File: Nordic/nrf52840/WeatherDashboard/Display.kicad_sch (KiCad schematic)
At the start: 14 parts, among them Q1 BSS138

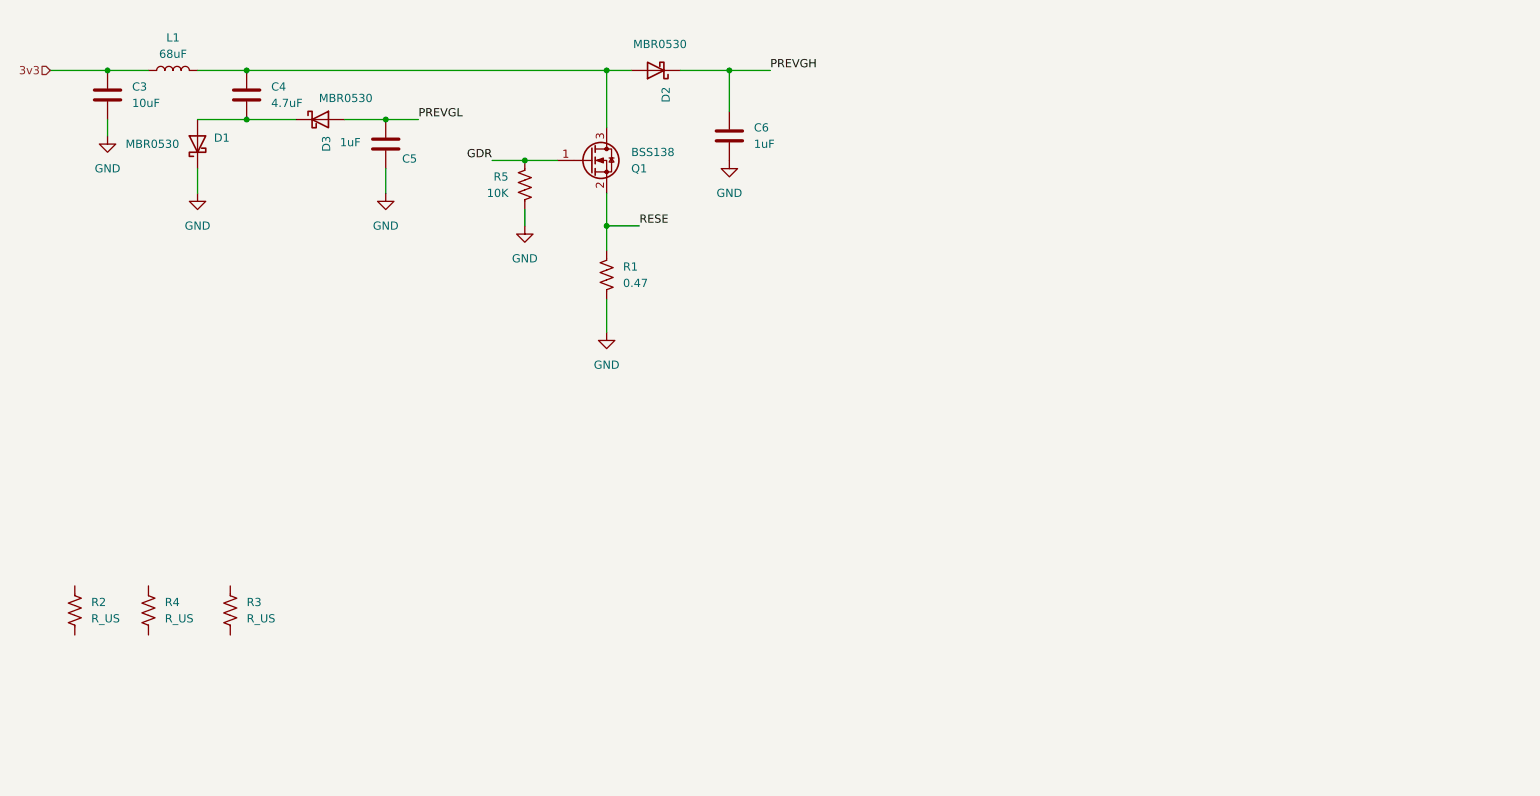
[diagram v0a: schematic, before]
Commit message: Display
Added fpc connector and power enable components
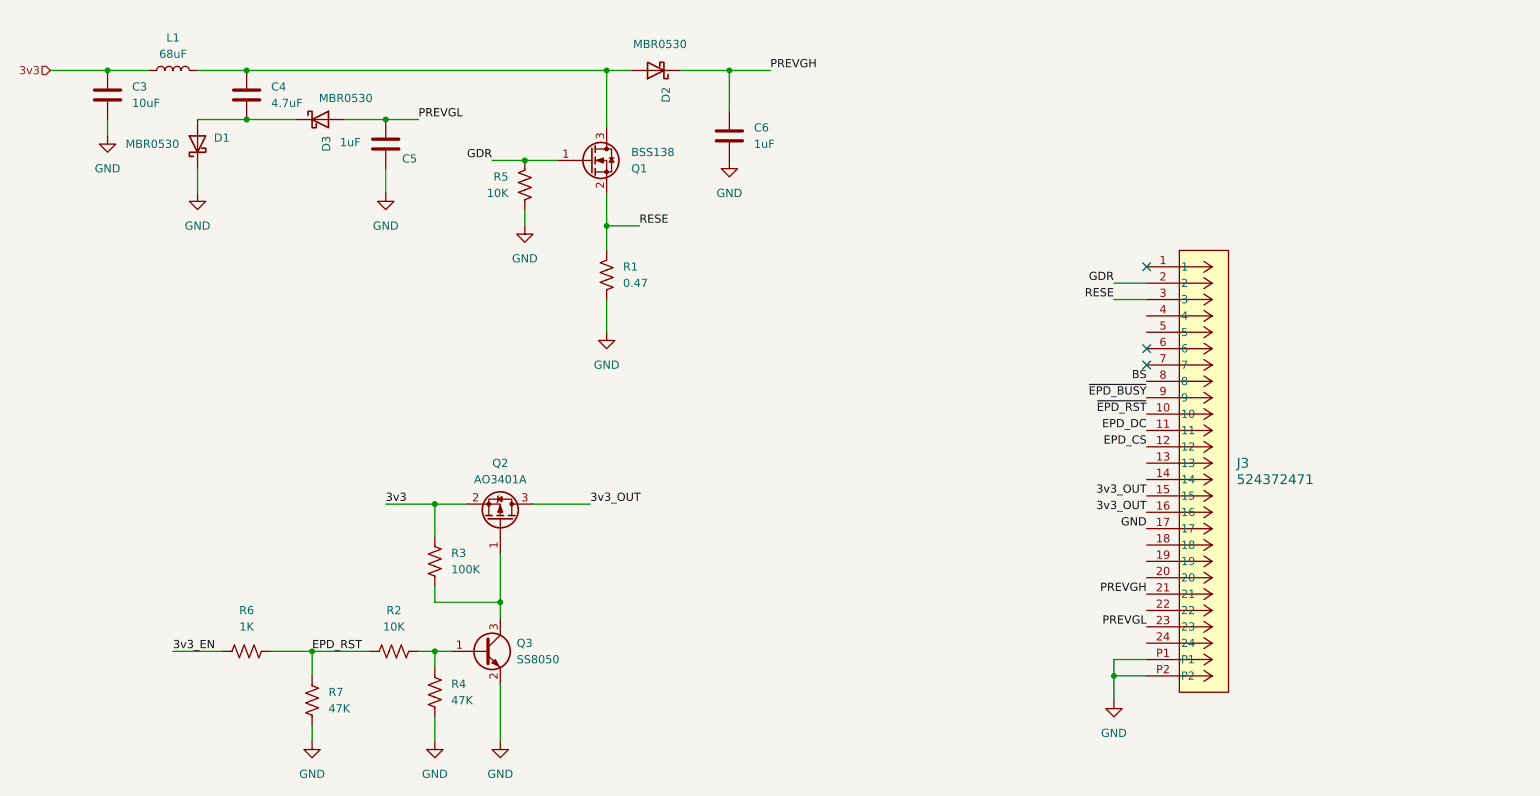
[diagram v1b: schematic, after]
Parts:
- added J3: 524372471, User_Footprint:CON_524372471_MOL, symbol _Connectors:524372471
- added Q2: AO3401A, Package_TO_SOT_SMD:SOT-23, symbol Transistor_FET:AO3401A
- added Q3: SS8050, Package_TO_SOT_SMD:SOT-23_Handsoldering, symbol Transistor_BJT:SS8050
- added R6: 1K, Resistor_SMD:R_0402_1005Metric_Pad0.72x0.64mm_HandSolder, symbol Device:R_US
- added R7: 47K, Resistor_SMD:R_0402_1005Metric_Pad0.72x0.64mm_HandSolder, symbol Device:R_US
- R2: value R_US -> 10K
- R3: value R_US -> 100K
- R4: value R_US -> 47K
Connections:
- net 3v3: now also R3.1, Q2.2 (S)
- net GDR: now also J3.2
- net GND: now also R4.2, J3.17, J3.P1, J3.P2, Q3.2 (E), R7.1
- net PREVGH: now also J3.21
- net PREVGL: now also J3.23
- net RESE: now also J3.3
- net at R3.2: now also Q2.1 (G), Q3.3 (C)
- net EPD_RST: now reaches R2.1
- net EPD_RST: now also R6.1, R7.2
- net at R2.2: now also R4.1, Q3.1 (B)
- new net 3v3_EN: R6.2
- new net 3v3_OUT: J3.15, J3.16, Q2.3 (D)
- new net BS: J3.8
- new net EPD_CS: J3.12
- new net EPD_DC: J3.11
- new net ~{EPD_BUSY}: J3.9
- new net ~{EPD_RST}: J3.10
- no-connect marks 0 -> 3
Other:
- moved on the sheet: R2, R3, R4

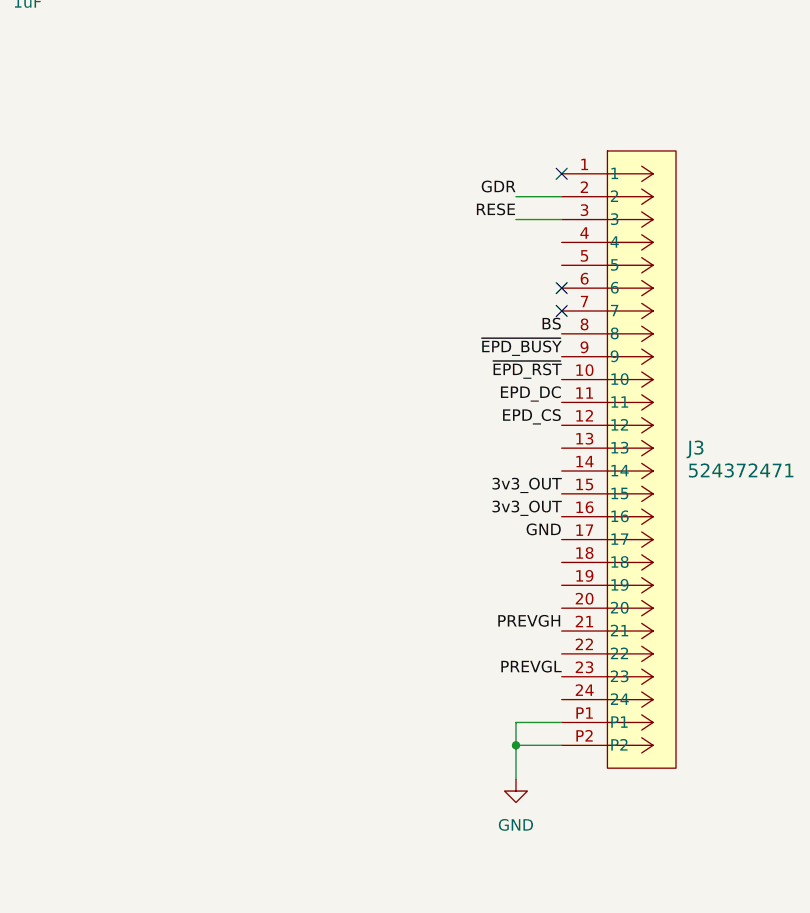
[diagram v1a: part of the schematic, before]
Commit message: pcie
added pcie connector
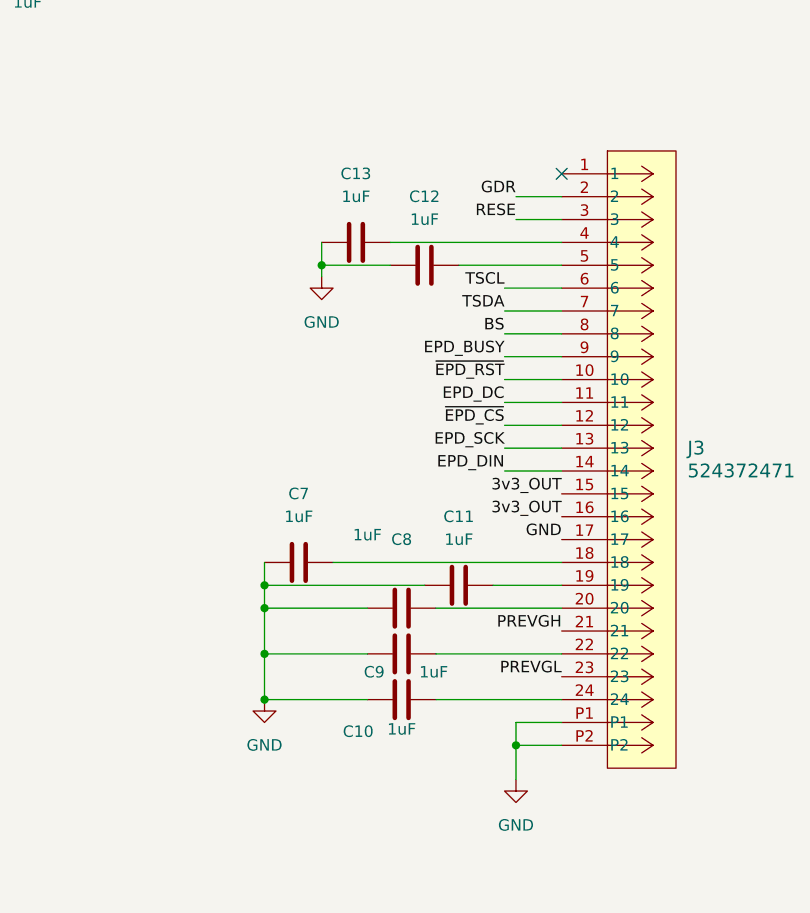
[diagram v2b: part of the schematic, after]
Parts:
- added C10, C11, C12, C13, C7, C8, C9: 1uF, Capacitor_SMD:C_0402_1005Metric_Pad0.74x0.62mm_HandSolder, symbol Device:C
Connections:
- net GND: now also C10.1, C11.1, C12.1, C13.1, C7.1, C8.1, C9.1
- net EPD_SCK: now reaches J3.13
- net EPD_DIN: now reaches J3.14
- net at J3.18: now also C7.2
- net at J3.19: now also C11.2
- net at J3.20: now also C8.2
- net at J3.22: now also C9.2
- net at J3.24: now also C10.2
- net at J3.4: now also C13.2
- net at J3.5: now also C12.2
- net TSCL: now reaches J3.6
- net TSDA: now reaches J3.7
- net EPD_CS renamed ~{EPD_CS}
- net ~{EPD_BUSY} renamed EPD_BUSY
- no-connect marks 3 -> 1

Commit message: pcie connector
Add connectins to the pcie connector
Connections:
- net EPD_BUSY: now also J3.14; no longer J3.9
- net EPD_DC: now also J3.12; no longer J3.11
- net EPD_DIN: now also J3.9; no longer J3.14
- net EPD_SCK: now also J3.10; no longer J3.13
- net TSCL: now also J3.7; no longer J3.6
- net TSDA: now also J3.6; no longer J3.7
- net ~{EPD_CS}: now also J3.11; no longer J3.12
- net ~{EPD_RST}: now also J3.13; no longer J3.10
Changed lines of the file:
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@@
-		)
-	)
-	(label "EPD_BUSY"
-		(at 187.96 85.09 180)
-		(effects
-			(font
-				(size 1.27 1.27)
-			)
-			(justify right bottom)
-		)
-	)
-	(label "3v3_EN"
-		(at 43.18 124.46 0)
-		(effects
-			(font
-				(size 1.27 1.27)
-			)
-			(justify left bottom)
-		)
-	)
-	(label "BS"
-		(at 187.96 82.55 180)
-		(effects
-			(font
-				(size 1.27 1.27)
-			)
-			(justify right bottom)
 		)
 	)
@@
 		)
 	)
-	(label "~{EPD_CS}"
-		(at 187.96 92.71 180)
-		(effects
-			(font
-				(size 1.27 1.27)
-			)
-			(justify right bottom)
-		)
-	)
 	(label "PREVGH"
 		(at 194.31 115.57 180)
@@
 		)
 	)
-	(label "EPD_DIN"
-		(at 187.96 97.79 180)
-		(effects
-			(font
-				(size 1.27 1.27)
-			)
-			(justify right bottom)
-		)
-	)
 	(label "GDR"
 		(at 92.71 48.26 180)
@@
 		)
 	)
-	(label "TSDA"
-		(at 187.96 80.01 180)
-		(effects
-			(font
-				(size 1.27 1.27)
-			)
-			(justify right bottom)
-		)
-	)
 	(label "GDR"
 		(at 189.23 67.31 180)
@@
 		)
 	)
-	(label "EPD_SCK"
-		(at 187.96 95.25 180)
-		(effects
-			(font
-				(size 1.27 1.27)
-			)
-			(justify right bottom)
-		)
-	)
 	(label "PREVGL"
 		(at 194.31 120.65 180)
@@
 		)
 	)
-	(label "TSCL"
-		(at 187.96 77.47 180)
-		(effects
-			(font
-				(size 1.27 1.27)
-			)
-			(justify right bottom)
-		)
-	)
 	(label "3v3"
 		(at 76.2 101.6 0)
@@
 		)
 	)
-	(label "~{EPD_RST}"
-		(at 187.96 87.63 180)
-		(effects
-			(font
-				(size 1.27 1.27)
-			)
-			(justify right bottom)
-		)
-	)
 	(label "RESE"
 		(at 189.23 69.85 180)
@@
 		)
 	)
-	(label "EPD_DC"
+	(hierarchical_label "BS"
+		(shape input)
+		(at 187.96 82.55 180)
+		(effects
+			(font
+				(size 1.27 1.27)
+			)
+			(justify right)
+		)
+	)
+	(hierarchical_label "EPD_DIN"
+		(shape input)
+		(at 187.96 85.09 180)
+		(effects
+			(font
+				(size 1.27 1.27)
+			)
+			(justify right)
+		)
+	)
+	(hierarchical_label "3v3"
+		(shape input)
+		(at 24.13 34.29 180)
+		(effects
+			(font
+				(size 1.27 1.27)
+			)
+			(justify right)
+		)
+	)
+	(hierarchical_label "GND"
+		(shape input)
+		(at 161.29 118.11 180)
+		(effects
+			(font
+				(size 1.27 1.27)
+			)
+			(justify right)
+		)
+	)
+	(hierarchical_label "~{EPD_RST}"
+		(shape input)
+		(at 187.96 95.25 180)
+		(effects
+			(font
+				(size 1.27 1.27)
+			)
+			(justify right)
+		)
+	)
+	(hierarchical_label "~{EPD_CS}"
+		(shape input)
 		(at 187.96 90.17 180)
 		(effects
@@
 				(size 1.27 1.27)
 			)
-			(justify right bottom)
-		)
-	)
-	(hierarchical_label "3v3"
-		(shape input)
-		(at 24.13 34.29 180)
-		(effects
-			(font
+			(justify right)
+		)
+	)
+	(hierarchical_label "EPD_DC"
+		(shape input)
+		(at 187.96 92.71 180)
+		(effects
+			(font
+				(size 1.27 1.27)
+			)
+			(justify right)
+		)
+	)
+	(hierarchical_label "EPD_BUSY"
+		(shape input)
+		(at 187.96 97.79 180)
+		(effects
+			(font
+				(size 1.27 1.27)
+			)
+			(justify right)
+		)
+	)
+	(hierarchical_label "TSDA"
+		(shape input)
+		(at 187.96 77.47 180)
+		(effects
+			(font
+				(size 1.27 1.27)
+			)
+			(justify right)
+		)
+	)
+	(hierarchical_label "TSCL"
+		(shape input)
+		(at 187.96 80.01 180)
+		(effects
+			(font
+				(size 1.27 1.27)
+			)
+			(justify right)
+		)
+	)
+	(hierarchical_label "3v3_EN"
+		(shape input)
+		(at 43.18 124.46 180)
+		(effects
+			(font
+				(size 1.27 1.27)
+			)
+			(justify right)
+		)
+	)
+	(hierarchical_label "EPD_SCK"
+		(shape input)
+		(at 187.96 87.63 180)
+		(effects
+			(font

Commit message: Layout
layout update
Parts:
- removed L1: 68uF, symbol Device:L
- added L1: SDE0805A-680K, User_Footprint:IND_SDE0805A-680K, symbol _Misc_Symbols:SDE0805A-680K
- added R10, R9: 0, Resistor_SMD:R_0402_1005Metric_Pad0.72x0.64mm_HandSolder, symbol Device:R_US
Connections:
- net 3v3: now also L1.1, R9.1
- net GND: now also R10.2
- net at C4.1, D2.2 (A), Q1.3 (D): now also L1.2
- net BS: no longer names the net of J3.8
- net BS: now also R10.1, R9.2
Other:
- moved on the sheet: C3

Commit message: layout
update layout for the pcie connector
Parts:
- added R17, R18: 10K, Resistor_SMD:R_0402_1005Metric_Pad0.72x0.64mm_HandSolder, symbol Device:R_US
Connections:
- net 3v3: now also R17.2, R18.2
- net TSCL: now also R18.1
- net TSDA: now also R17.1
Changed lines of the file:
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@@
+	)
+	(junction
+		(at 241.3 44.45)
+		(diameter 0)
+		(color 0 0 0 0)
 	)
 	(junction
@@
 	(wire
 		(pts
+			(xy 234.95 52.07) (xy 234.95 55.88)
+		)
+		(stroke
+			(width 0)
+			(type default)
+		)
+	)
+	(wire
+		(pts
 			(xy 64.77 135.89) (xy 64.77 138.43)
 		)
@@
 	(wire
 		(pts
+			(xy 246.38 52.07) (xy 246.38 55.88)
+		)
+		(stroke
+			(width 0)
+			(type default)
+		)
+	)
+	(wire
+		(pts
 			(xy 81.28 124.46) (xy 83.82 124.46)
 		)
@@
 	(wire
 		(pts
+			(xy 234.95 55.88) (xy 233.68 55.88)
+		)
+		(stroke
+			(width 0)
+			(type default)
+		)
+	)
+	(wire
+		(pts
 			(xy 189.23 67.31) (xy 194.31 67.31)
 		)
@@
 	(wire
 		(pts
+			(xy 234.95 44.45) (xy 241.3 44.45)
+		)
+		(stroke
+			(width 0)
+			(type default)
+		)
+	)
+	(wire
+		(pts
 			(xy 187.96 87.63) (xy 194.31 87.63)
 		)
@@
 	(wire
 		(pts
+			(xy 246.38 55.88) (xy 247.65 55.88)
+		)
+		(stroke
+			(width 0)
+			(type default)
+		)
+	)
+	(wire
+		(pts
 			(xy 180.34 118.11) (xy 194.31 118.11)
 		)
@@
 	(wire
 		(pts
+			(xy 241.3 38.1) (xy 241.3 44.45)
+		)
+		(stroke
+			(width 0)
+			(type default)
+		)
+	)
+	(wire
+		(pts
 			(xy 180.34 113.03) (xy 194.31 113.03)
 		)
@@
 		(pts
 			(xy 43.18 124.46) (xy 50.8 124.46)
+		)
+		(stroke
+			(width 0)
+			(type default)
+		)
+	)
+	(wire
+		(pts
+			(xy 241.3 44.45) (xy 246.38 44.45)
 		)
 		(stroke
@@
 		)
 	)
+	(label "3v3"
+		(at 241.3 38.1 0)
+		(effects
+			(font
+				(size 1.27 1.27)
+			)
+			(justify left bottom)
+		)
+	)
 	(label "GDR"
 		(at 189.23 67.31 180)
@@
 		)
 	)
+	(label "TSDA"
+		(at 233.68 55.88 180)
+		(effects
+			(font
+				(size 1.27 1.27)
+			)
+			(justify right bottom)
+		)
+	)
 	(label "RESE"
 		(at 115.57 58.42 0)
@@
 	(label "PREVGL"
 		(at 81.28 41.91 0)
+		(effects
+			(font
+				(size 1.27 1.27)
+			)
+			(justify left bottom)
+		)
+	)
+	(label "TSCL"
+		(at 247.65 55.88 0)
 		(effects
 			(font
@@
 	)
 	(symbol
+		(lib_id "Device:R_US")
+		(at 234.95 48.26 180)
+		(unit 1)
+		(exclude_from_sim no)
+		(in_bom yes)
+		(on_board yes)
+		(dnp no)
+		(fields_autoplaced yes)
+		(property "Reference" "R17"
+			(at 237.49 46.9899 0)
+			(effects
+				(font
+					(size 1.27 1.27)
+				)
+				(justify right)
+			)
+		)
+		(property "Value" "10K"
+			(at 237.49 49.5299 0)
+			(effects
+				(font
+					(size 1.27 1.27)
+				)
+				(justify right)
+			)
+		)
+		(property "Footprint" "Resistor_SMD:R_0402_1005Metric_Pad0.72x0.64mm_HandSolder"
+			(at 233.934 48.006 90)
+			(effects
+				(font
+					(size 1.27 1.27)
+				)
+				(hide yes)
+			)
+		)
+		(property "Datasheet" "~"
+			(at 234.95 48.26 0)
+			(effects
+				(font
+					(size 1.27 1.27)
+				)
+				(hide yes)
+			)
+		)
+		(property "Description" "Resistor, US symbol"
+			(at 234.95 48.26 0)
+			(effects
+				(font
+					(size 1.27 1.27)
+				)
+				(hide yes)
+			)
+		)
+		(pin "2"
+		)
+		(pin "1"
+		)
+		(instances
+			(project "WeatherDashboard"
+				(path "/189808bb-364f-4c11-a922-cc9d9f33a674/467bc621-b4b5-45fe-9f37-7652e0bd9a4d"
+					(reference "R17")
+					(unit 1)
+				)
+			)
+		)
+	)
+	(symbol
 		(lib_id "power:GND")
 		(at 26.67 45.72 0)
@@
 					(unit 1)
 				)
+			)
+		)
+	)
+	(symbol
+		(lib_id "Device:R_US")
+		(at 246.38 48.26 180)
+		(unit 1)
+		(exclude_from_sim no)
+		(in_bom yes)
+		(on_board yes)
+		(dnp no)
+		(fields_autoplaced yes)
+		(property "Reference" "R18"
+			(at 248.92 46.9899 0)
+			(effects
+				(font
+					(size 1.27 1.27)
+				)
+				(justify right)
+			)
+		)
+		(property "Value" "10K"
+			(at 248.92 49.5299 0)
+			(effects
+				(font
+					(size 1.27 1.27)
+				)
+				(justify right)
+			)
+		)
+		(property "Footprint" "Resistor_SMD:R_0402_1005Metric_Pad0.72x0.64mm_HandSolder"
+			(at 245.364 48.006 90)
+			(effects
+				(font
+					(size 1.27 1.27)
+				)
+				(hide yes)
+			)
+		)
+		(property "Datasheet" "~"
+			(at 246.38 48.26 0)
+			(effects
+				(font
+					(size 1.27 1.27)
+				)
+				(hide yes)
+			)
+		)
+		(property "Description" "Resistor, US symbol"
+			(at 246.38 48.26 0)
+			(effects
+				(font
+					(size 1.27 1.27)
+				)
+				(hide yes)
+			)
+		)
+		(pin "2"
+		)
+		(pin "1"
+		)
+		(instances
+			(project "WeatherDashboard"
+				(path "/189808bb-364f-4c11-a922-cc9d9f33a674/467bc621-b4b5-45fe-9f37-7652e0bd9a4d"
+					(reference "R18")
+					(unit 1)
+				)
